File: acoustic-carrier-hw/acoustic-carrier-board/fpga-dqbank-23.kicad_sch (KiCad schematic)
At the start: 10 parts, among them IC1 ECP5-BGA256

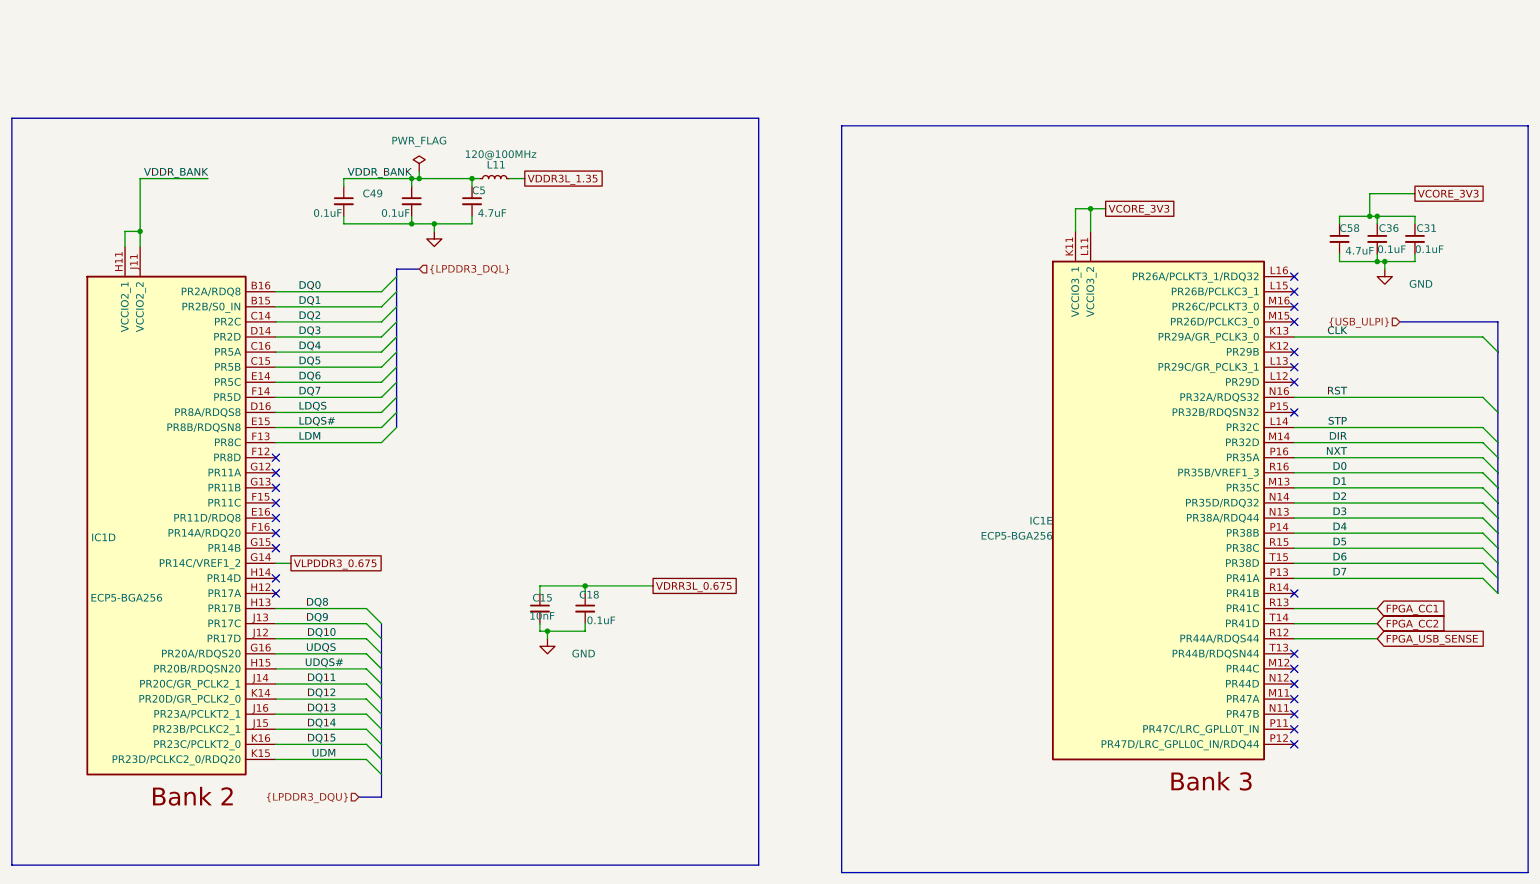
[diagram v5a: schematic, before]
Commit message: [carrier] Added testpoints
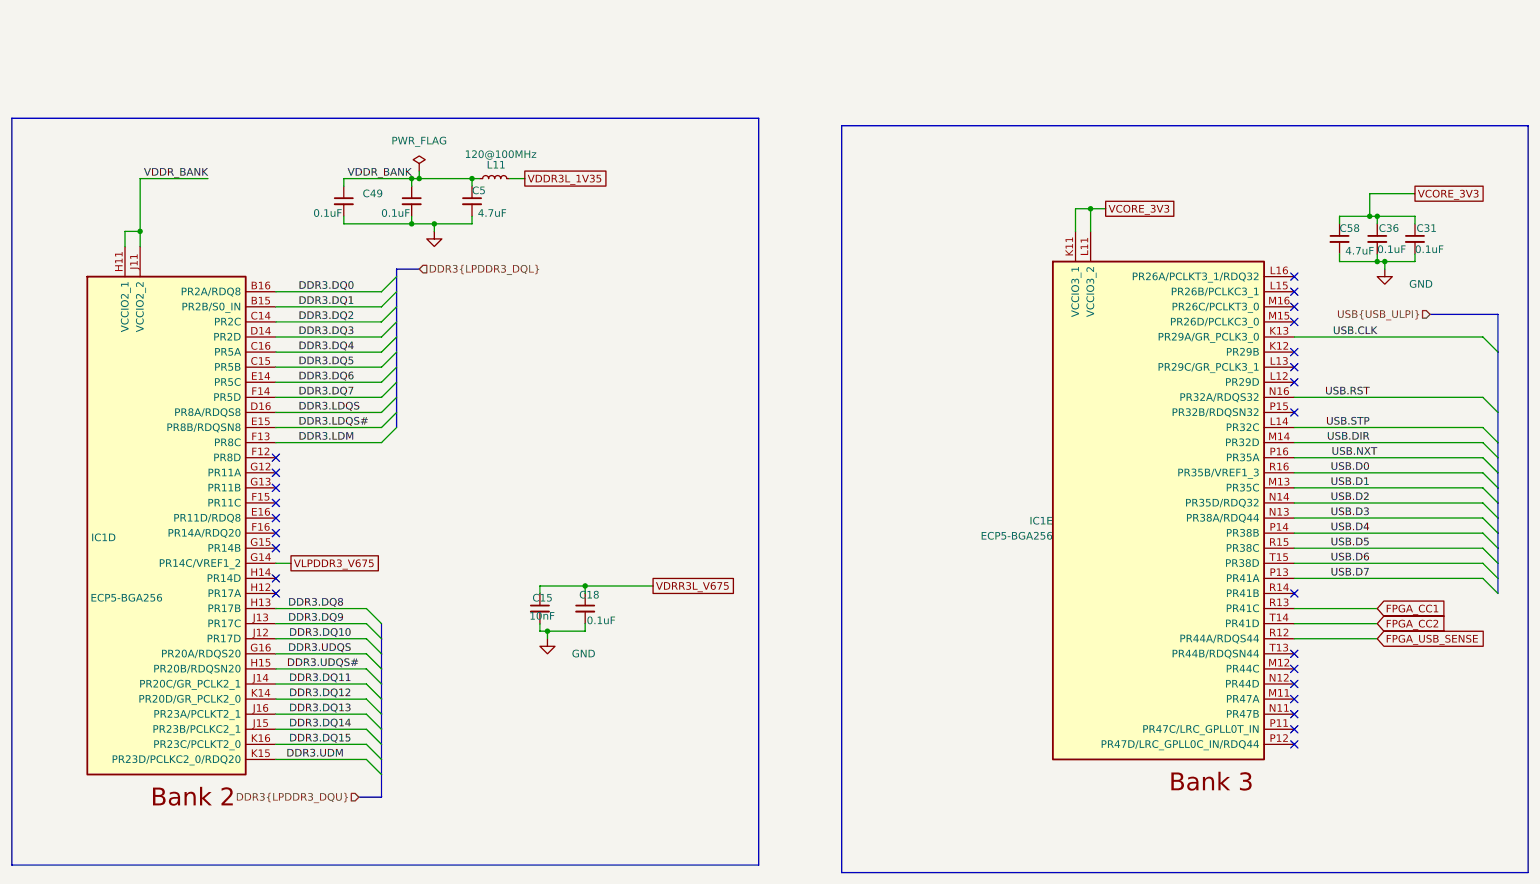
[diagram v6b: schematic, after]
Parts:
- C15: LPN CL05B103KB5NNNC -> C15195; MPN C15195 -> CL05B103KB5NNNC
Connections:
- net CLK renamed USB.CLK
- net D0 renamed USB.D0
- net D1 renamed USB.D1
- net D2 renamed USB.D2
- net D3 renamed USB.D3
- net D4 renamed USB.D4
- net D5 renamed USB.D5
- net D6 renamed USB.D6
- net D7 renamed USB.D7
- net DIR renamed USB.DIR
- net DQ0 renamed DDR3.DQ0
- net DQ1 renamed DDR3.DQ1
- net DQ10 renamed DDR3.DQ10
- net DQ11 renamed DDR3.DQ11
- net DQ12 renamed DDR3.DQ12
- net DQ13 renamed DDR3.DQ13
- net DQ14 renamed DDR3.DQ14
- net DQ15 renamed DDR3.DQ15
- net DQ2 renamed DDR3.DQ2
- net DQ3 renamed DDR3.DQ3
- net DQ4 renamed DDR3.DQ4
- net DQ5 renamed DDR3.DQ5
- net DQ6 renamed DDR3.DQ6
- net DQ7 renamed DDR3.DQ7
- net DQ8 renamed DDR3.DQ8
- net DQ9 renamed DDR3.DQ9
- net LDM renamed DDR3.LDM
- net LDQS renamed DDR3.LDQS
- net LDQS# renamed DDR3.LDQS#
- net NXT renamed USB.NXT
- net RST renamed USB.RST
- net STP renamed USB.STP
- net UDM renamed DDR3.UDM
- net UDQS renamed DDR3.UDQS
- net UDQS# renamed DDR3.UDQS#
- net VDDR3L_1.35 renamed VDDR3L_1V35
- net VDRR3L_0.675 renamed VDRR3L_V675
- net VLPDDR3_0.675 renamed VLPDDR3_V675

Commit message: [carrier] Finished rough layout, p (put together according to component category
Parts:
- renumbered C49 to C501, C57 to C502, C5 to C503, C58 to C504, C36 to C505, C31 to C506, C15 to C507, C18 to C508, L11 to L501
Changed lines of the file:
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@@
 		(on_board yes)
 		(dnp no)
-		(property "Reference" "#PWR06"
+		(property "Reference" "#PWR0503"
 			(at 116.84 127 0)
 			(effects
@@
 			(project "acoustic-carrier-board"
 				(path "/25b015c9-ab13-4427-b72c-b6f348597100/b53b103a-6456-47cb-a34f-3ea275fe1ee5"
-					(reference "#PWR06")
+					(reference "#PWR0503")
 					(unit 1)
 				)
@@
 		(on_board yes)
 		(dnp no)
-		(property "Reference" "C57"
+		(property "Reference" "C502"
 			(at 100.584 45.72 0)
 			(effects
@@
 			(project "acoustic-carrier-board"
 				(path "/25b015c9-ab13-4427-b72c-b6f348597100/b53b103a-6456-47cb-a34f-3ea275fe1ee5"
-					(reference "C57")
+					(reference "C502")
 					(unit 1)
 				)
@@
 		(on_board yes)
 		(dnp no)
-		(property "Reference" "C31"
+		(property "Reference" "C506"
 			(at 263.144 51.562 0)
 			(effects
@@
 			(project "acoustic-carrier-board"
 				(path "/25b015c9-ab13-4427-b72c-b6f348597100/b53b103a-6456-47cb-a34f-3ea275fe1ee5"
-					(reference "C31")
+					(reference "C506")
 					(unit 1)
 				)
@@
 		(on_board yes)
 		(dnp no)
-		(property "Reference" "#PWR09"
+		(property "Reference" "#PWR0501"
 			(at 97.79 58.42 0)
 			(effects
@@
 			(project "acoustic-carrier-board"
 				(path "/25b015c9-ab13-4427-b72c-b6f348597100/b53b103a-6456-47cb-a34f-3ea275fe1ee5"
-					(reference "#PWR09")
+					(reference "#PWR0501")
 					(unit 1)
 				)
@@
 		(on_board yes)
 		(dnp no)
-		(property "Reference" "C58"
+		(property "Reference" "C504"
 			(at 250.19 51.562 0)
 			(effects
@@
 			(project "acoustic-carrier-board"
 				(path "/25b015c9-ab13-4427-b72c-b6f348597100/b53b103a-6456-47cb-a34f-3ea275fe1ee5"
-					(reference "C58")
+					(reference "C504")
 					(unit 1)
 				)
@@
 		(dnp no)
 		(fields_autoplaced yes)
-		(property "Reference" "#FLG017"
+		(property "Reference" "#FLG0501"
 			(at 95.25 40.005 0)
 			(effects
@@
 			(project "acoustic-carrier-board"
 				(path "/25b015c9-ab13-4427-b72c-b6f348597100/b53b103a-6456-47cb-a34f-3ea275fe1ee5"
-					(reference "#FLG017")
+					(reference "#FLG0501")
 					(unit 1)
 				)
@@
 		(on_board yes)
 		(dnp no)
-		(property "Reference" "L11"
+		(property "Reference" "L501"
 			(at 108.204 40.894 90)
 			(effects
@@
 			(project "acoustic-carrier-board"
 				(path "/25b015c9-ab13-4427-b72c-b6f348597100/b53b103a-6456-47cb-a34f-3ea275fe1ee5"
-					(reference "L11")
+					(reference "L501")
 					(unit 1)
 				)
@@
 		(on_board yes)
 		(dnp no)
-		(property "Reference" "C15"
+		(property "Reference" "C507"
 			(at 114.3 113.792 0)
 			(effects
@@
 			(project "acoustic-carrier-board"
 				(path "/25b015c9-ab13-4427-b72c-b6f348597100/b53b103a-6456-47cb-a34f-3ea275fe1ee5"
-					(reference "C15")
+					(reference "C507")
 					(unit 1)
 				)
@@
 		(on_board yes)
 		(dnp no)
-		(property "Reference" "#PWR015"
+		(property "Reference" "#PWR0502"
 			(at 257.81 64.77 0)
 			(effects
@@
 			(project "acoustic-carrier-board"
 				(path "/25b015c9-ab13-4427-b72c-b6f348597100/b53b103a-6456-47cb-a34f-3ea275fe1ee5"
-					(reference "#PWR015")
+					(reference "#PWR0502")
 					(unit 1)
 				)
@@
 		(on_board yes)
 		(dnp no)
-		(property "Reference" "C36"
+		(property "Reference" "C505"
 			(at 256.794 51.562 0)
 			(effects
@@
 			(project "acoustic-carrier-board"
 				(path "/25b015c9-ab13-4427-b72c-b6f348597100/b53b103a-6456-47cb-a34f-3ea275fe1ee5"
-					(reference "C36")
+					(reference "C505")
 					(unit 1)
 				)
@@
 		(on_board yes)
 		(dnp no)
-		(property "Reference" "C5"
+		(property "Reference" "C503"
 			(at 104.14 45.212 0)
 			(effects
@@
 			(project "acoustic-carrier-board"
 				(path "/25b015c9-ab13-4427-b72c-b6f348597100/b53b103a-6456-47cb-a34f-3ea275fe1ee5"
-					(reference "C5")
+					(reference "C503")
 					(unit 1)
 				)
@@
 		(on_board yes)
 		(dnp no)
-		(property "Reference" "C18"
+		(property "Reference" "C508"
 			(at 122.174 113.284 0)
 			(effects
@@
 			(project "acoustic-carrier-board"
 				(path "/25b015c9-ab13-4427-b72c-b6f348597100/b53b103a-6456-47cb-a34f-3ea275fe1ee5"
-					(reference "C18")
+					(reference "C508")
 					(unit 1)
 				)
@@
 		(on_board yes)
 		(dnp no)
-		(property "Reference" "C49"
+		(property "Reference" "C501"
 			(at 89.154 45.72 0)
 			(effects
@@
 			(project "acoustic-carrier-board"
 				(path "/25b015c9-ab13-4427-b72c-b6f348597100/b53b103a-6456-47cb-a34f-3ea275fe1ee5"
-					(reference "C49")
+					(reference "C501")
 					(unit 1)
 				)

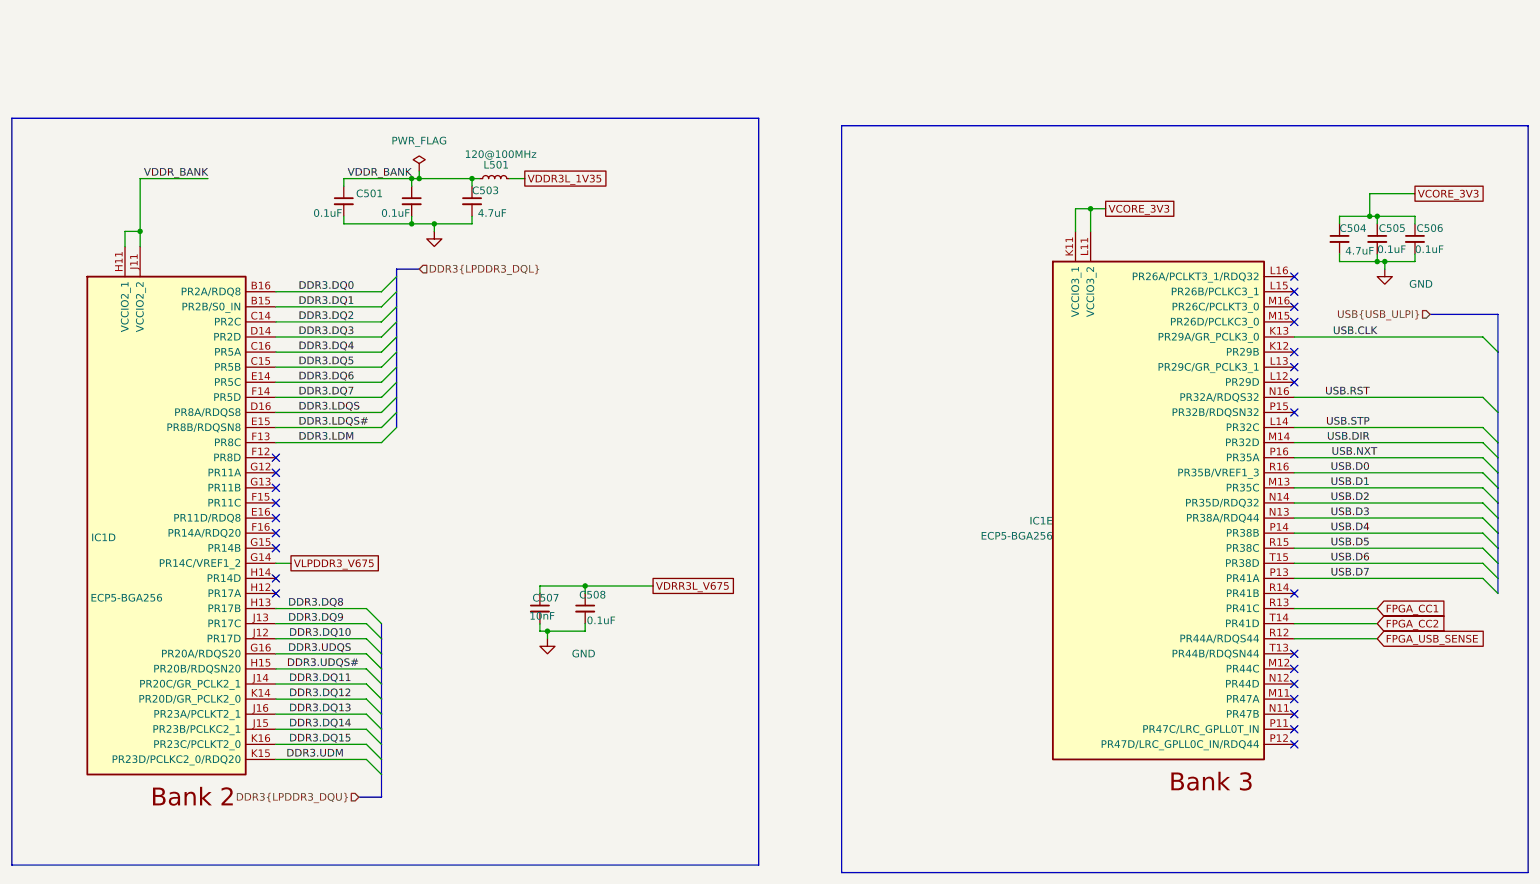
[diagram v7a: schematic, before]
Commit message: [¢arrier] Added netties and determined trace geometry for 50 ohms SE / 100 ohms DIFF impedance (next) reset the appropriate DQS group signals, RGMII and USB signals
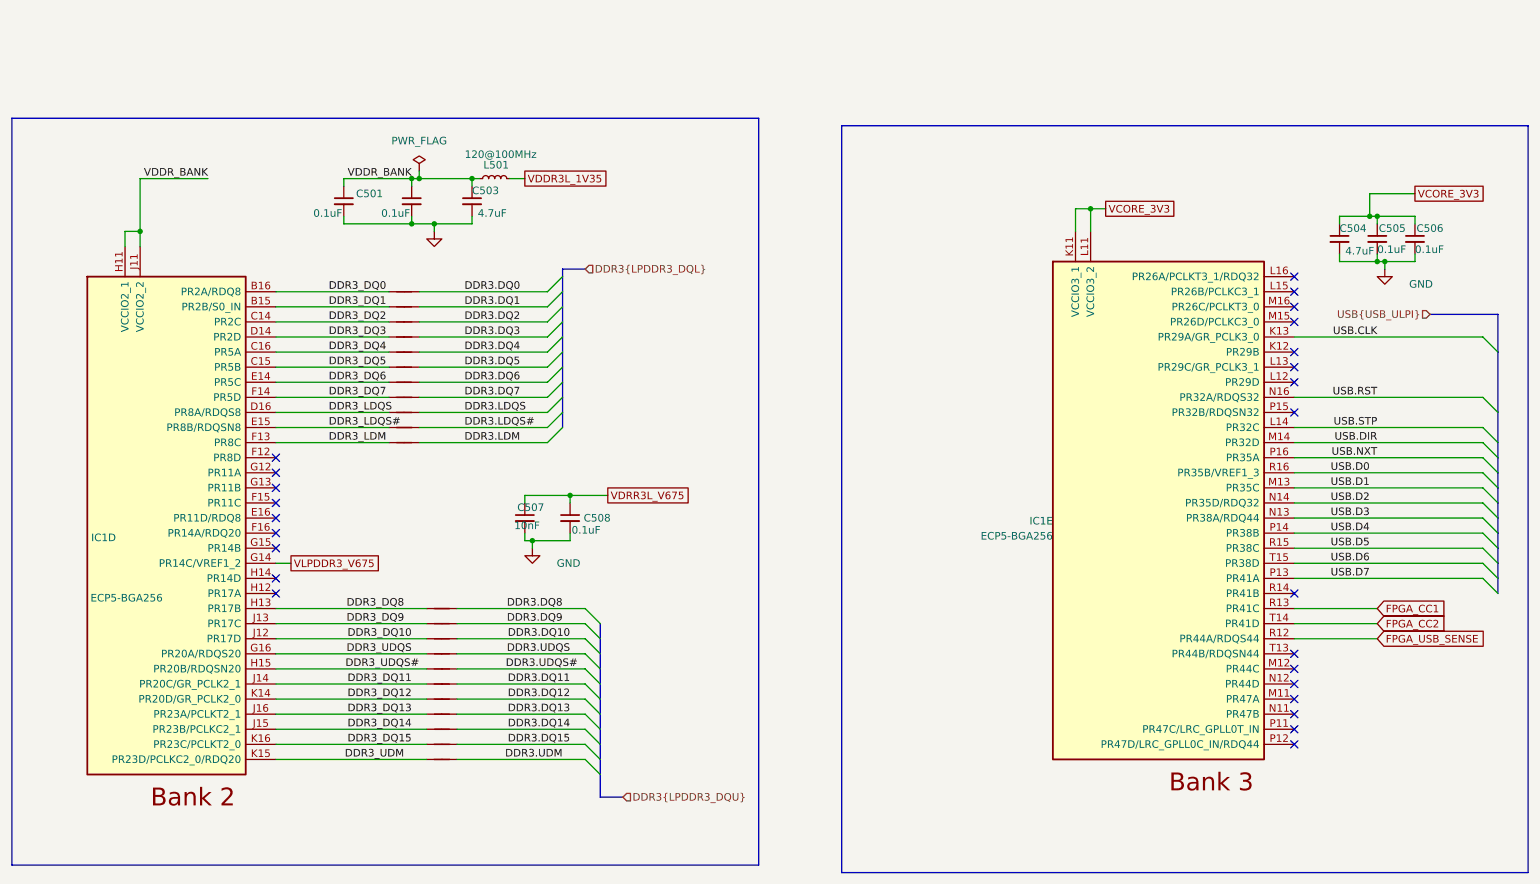
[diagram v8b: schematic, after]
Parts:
- added NT502, NT503, NT504, NT507, NT508, NT509, NT510, NT511, NT513, NT514, NT515, NT516, NT517, NT518, NT519, NT520, NT523, NT524: NetTie_2, iw-misc:NetTie-2_SMD_Pad0.1565mm, symbol Device:NetTie_2
- added NT505, NT506, NT521, NT522: NetTie_2, iw-misc:NetTie-2_SMD_Pad0.1240mm, symbol Device:NetTie_2
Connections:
- net DDR3.DQ0: now also NT514.2; no longer IC1.B16 (PR2A/RDQ8)
- net DDR3.DQ1: now also NT515.2; no longer IC1.B15 (PR2B/S0_IN)
- net DDR3.DQ10: now also NT523.2; no longer IC1.J12 (PR17D)
- net DDR3.DQ11: now also NT502.2; no longer IC1.J14 (PR20C/GR_PCLK2_1)
- net DDR3.DQ12: now also NT507.2; no longer IC1.K14 (PR20D/GR_PCLK2_0)
- net DDR3.DQ13: now also NT508.2; no longer IC1.J16 (PR23A/PCLKT2_1)
- net DDR3.DQ14: now also NT509.2; no longer IC1.J15 (PR23B/PCLKC2_1)
- net DDR3.DQ15: now also NT510.2; no longer IC1.K16 (PR23C/PCLKT2_0)
- net DDR3.DQ2: now also NT516.2; no longer IC1.C14 (PR2C)
- net DDR3.DQ3: now also NT517.2; no longer IC1.D14 (PR2D)
- net DDR3.DQ4: now also NT518.2; no longer IC1.C16 (PR5A)
- net DDR3.DQ5: now also NT519.2; no longer IC1.C15 (PR5B)
- net DDR3.DQ6: now also NT520.2; no longer IC1.E14 (PR5C)
- net DDR3.DQ7: now also NT524.2; no longer IC1.F14 (PR5D)
- net DDR3.DQ8: now also NT503.2; no longer IC1.H13 (PR17B)
- net DDR3.DQ9: now also NT504.2; no longer IC1.J13 (PR17C)
- net DDR3.LDM: now also NT513.2; no longer IC1.F13 (PR8C)
- net DDR3.LDQS: now also NT521.2; no longer IC1.D16 (PR8A/RDQS8)
- net DDR3.LDQS#: now also NT522.2; no longer IC1.E15 (PR8B/RDQSN8)
- net DDR3.UDM: now also NT511.2; no longer IC1.K15 (PR23D/PCLKC2_0/RDQ20)
- net DDR3.UDQS: now also NT505.2; no longer IC1.G16 (PR20A/RDQS20)
- net DDR3.UDQS#: now also NT506.2; no longer IC1.H15 (PR20B/RDQSN20)
- new net DDR3_DQ0: IC1.B16 (PR2A/RDQ8), NT514.1
- new net DDR3_DQ1: IC1.B15 (PR2B/S0_IN), NT515.1
- new net DDR3_DQ10: IC1.J12 (PR17D), NT523.1
- new net DDR3_DQ11: IC1.J14 (PR20C/GR_PCLK2_1), NT502.1
- new net DDR3_DQ12: IC1.K14 (PR20D/GR_PCLK2_0), NT507.1
- new net DDR3_DQ13: IC1.J16 (PR23A/PCLKT2_1), NT508.1
- new net DDR3_DQ14: IC1.J15 (PR23B/PCLKC2_1), NT509.1
- new net DDR3_DQ15: IC1.K16 (PR23C/PCLKT2_0), NT510.1
- new net DDR3_DQ2: IC1.C14 (PR2C), NT516.1
- new net DDR3_DQ3: IC1.D14 (PR2D), NT517.1
- new net DDR3_DQ4: IC1.C16 (PR5A), NT518.1
- new net DDR3_DQ5: IC1.C15 (PR5B), NT519.1
- new net DDR3_DQ6: IC1.E14 (PR5C), NT520.1
- new net DDR3_DQ7: IC1.F14 (PR5D), NT524.1
- new net DDR3_DQ8: IC1.H13 (PR17B), NT503.1
- new net DDR3_DQ9: IC1.J13 (PR17C), NT504.1
- new net DDR3_LDM: IC1.F13 (PR8C), NT513.1
- new net DDR3_LDQS: IC1.D16 (PR8A/RDQS8), NT521.1
- new net DDR3_LDQS#: IC1.E15 (PR8B/RDQSN8), NT522.1
- new net DDR3_UDM: IC1.K15 (PR23D/PCLKC2_0/RDQ20), NT511.1
- new net DDR3_UDQS: IC1.G16 (PR20A/RDQS20), NT505.1
- new net DDR3_UDQS#: IC1.H15 (PR20B/RDQSN20), NT506.1
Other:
- moved on the sheet: C507, C508
